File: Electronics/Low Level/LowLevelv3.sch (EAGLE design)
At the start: 66 parts, among them IC1_2515 MCP2515, IC2_2551 MCP2551DIL08, IC3_4802 MCP4802, Q1 16MHz, T1 2N3904, T2 2N3904, X1 284512-4, X3 Motor, X4 CLICK

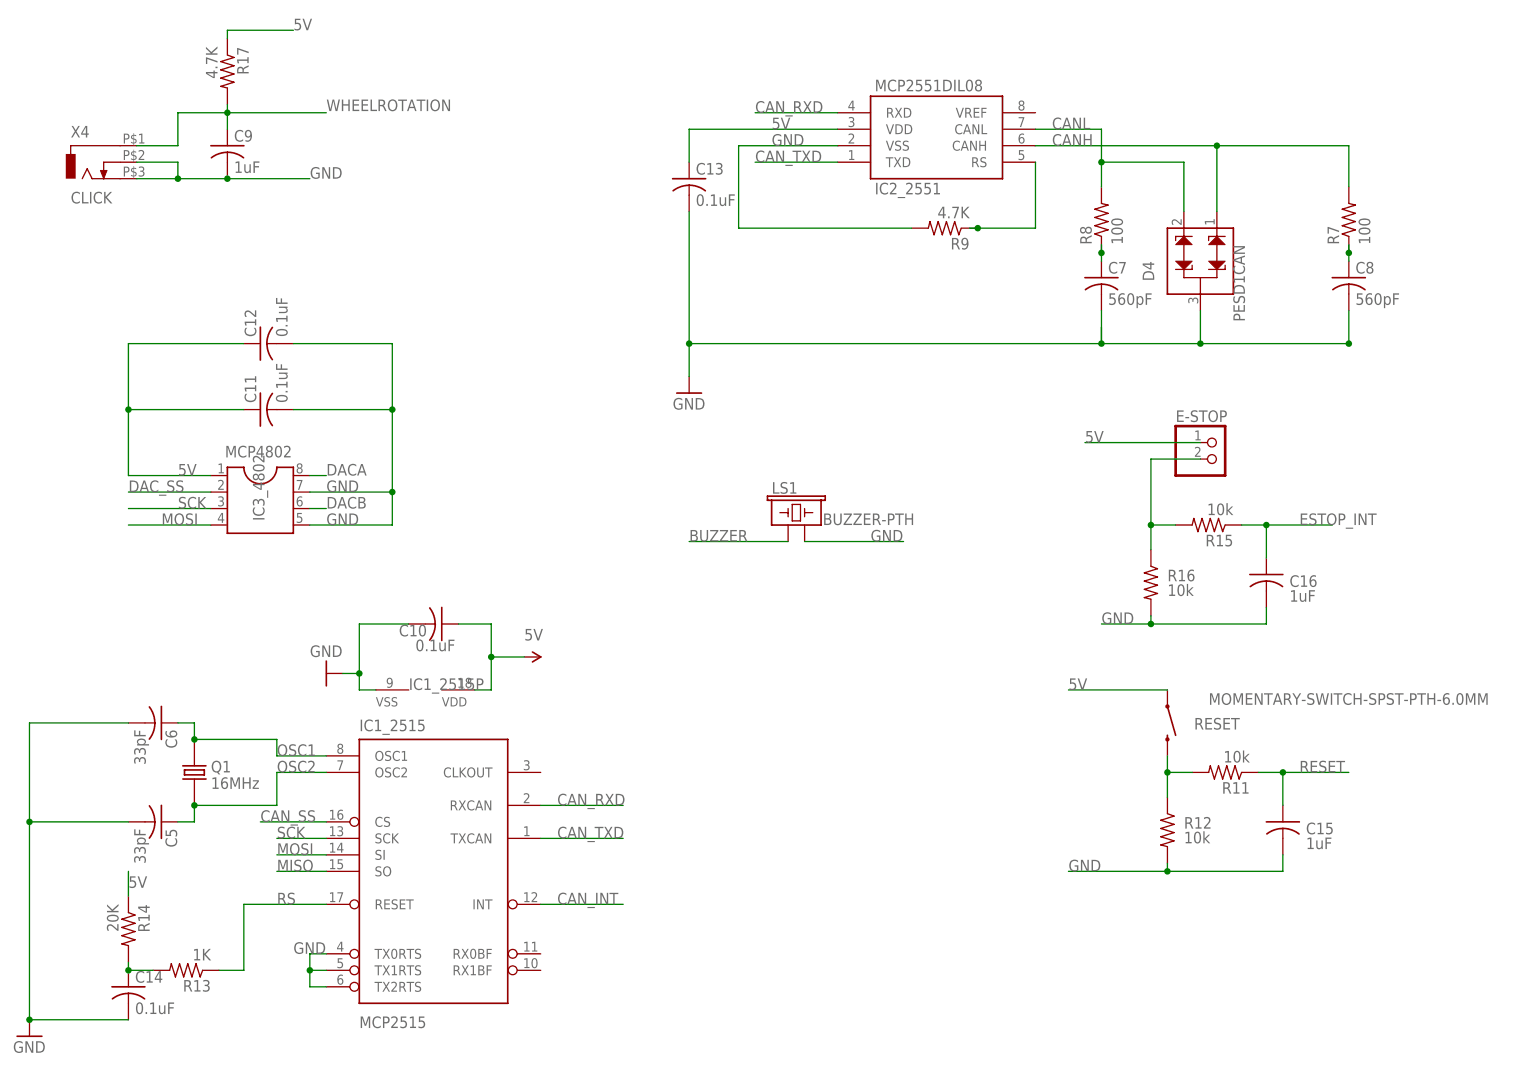
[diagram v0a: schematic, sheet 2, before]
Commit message: LLBv3 corrections
Fixed silk-via overlapping regions.
Fixed reset button schematic/wiring, now connects reset to ground.
Swapped CAN differential pair pinout by fixing the part in the library and re-routing the board.
Moved some surface mount parts to better propagate the ground plane.

Added on-silkscreen documentation for CAN and relay pinouts.
Added power-OK led and its resistor.
Changed board outline, reduced area and added two corner cuts.
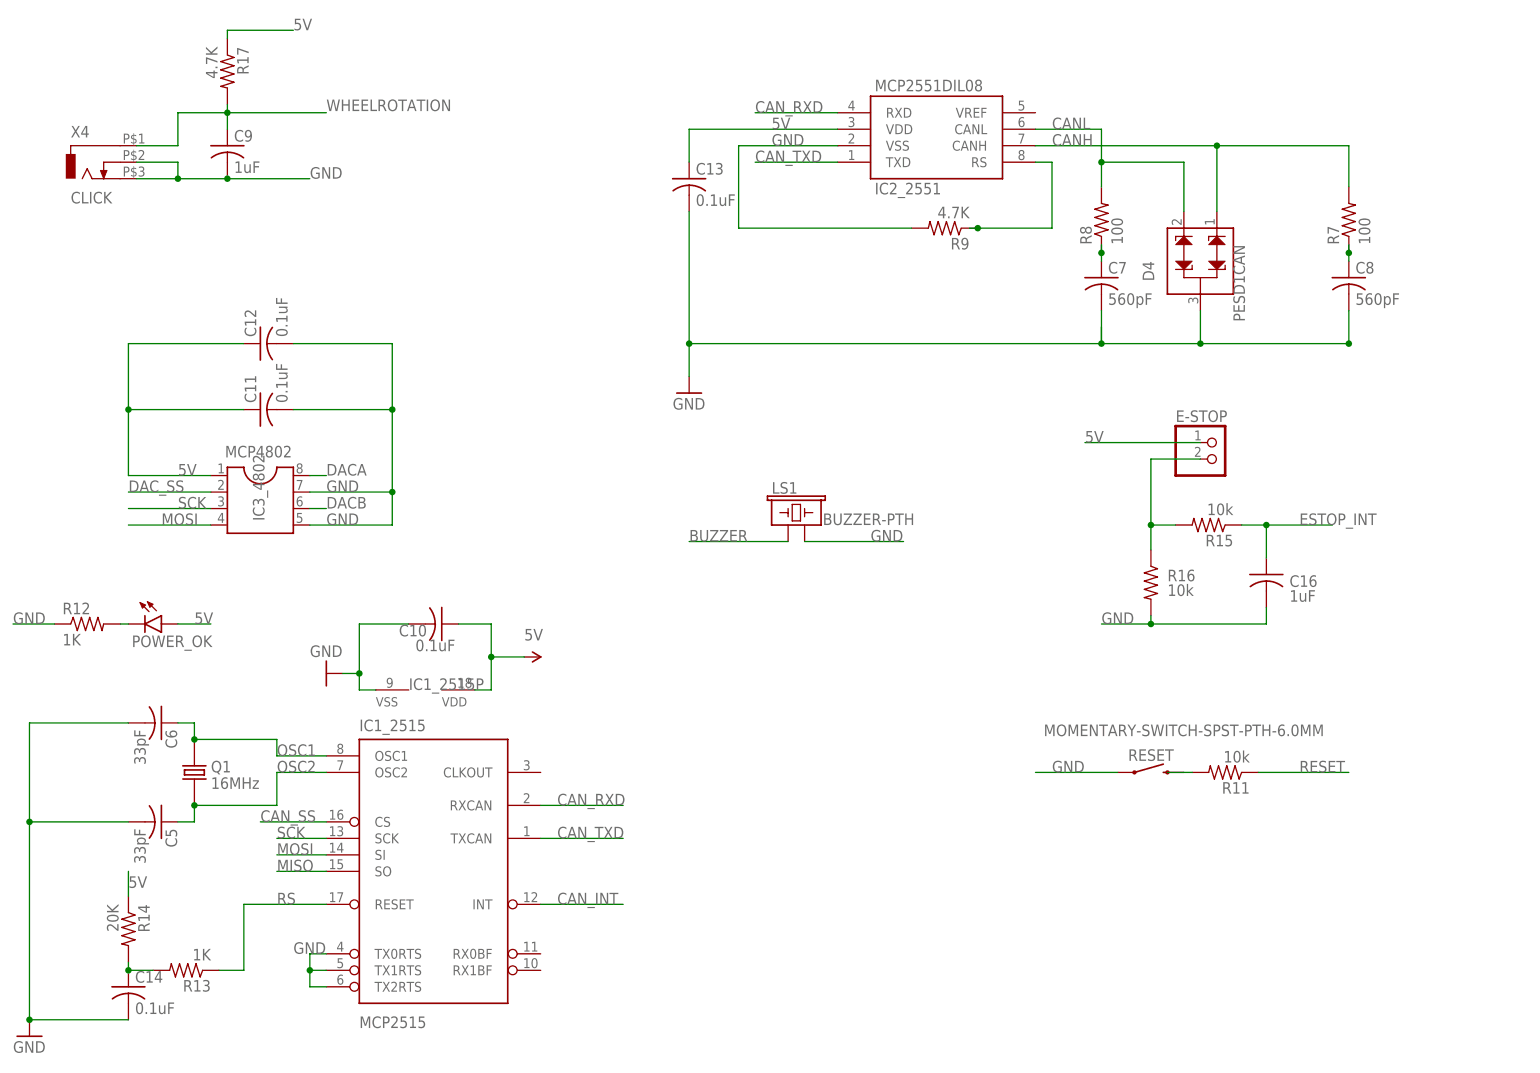
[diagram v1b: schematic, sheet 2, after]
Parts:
- removed C15: 1uF, resistor:C-USC1206
- added POWER_OK: (no value), led:LED3MM
- ICSP: value ICSP -> 2x3
- R12: value 10k -> 1K
- renumbered CANBUS to CAN/UART
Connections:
- new net N$11: POWER_OK.C, R12.2
- net 12V: now also X1.4; no longer X1.1
- net 24V: now also X1.3; no longer X1.2
- net 5V: now also POWER_OK.A; no longer RESET.1
- net GND: now also R12.1, RESET.1; no longer C15.2, R12.2
- net N$1: no longer R12.1
- net RESET: no longer C15.1
- net SOLENOID_COMMON: now also X1.1; no longer X1.4
- net SOLENOID_OUT: now also X1.2; no longer X1.3
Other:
- moved on the sheet: D1, R12, RESET, X1

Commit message: LLBv3.1 changes
Rerouted high-current relay circuit to handle swapped NC/NO pins.
Replaced 10-pin connector with 8-pin RJ45 modular jack. Expensive mistake.
Added debug LED on pin D13.
Added test points for steering header.
Silkscreen and routing corrections.
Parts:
- removed C2, C4: 1uF, resistor:C-USC1206
- removed R4: 4.7K, resistor:R-US_R1206
- removed STEERING_IO: 5-104069-4, elcanoParts:5-104069-4
- added DEBUG: (no value), led:LED3MM
- added STEERING: RJ45-8L-B, elcanoParts:RJ45-8L-B
- added TP1, TP2, TP3, TP4, TP5: PTR1PAD1-17, testpad:PTR1PAD1-17
- R2: value 4.7K -> 1K
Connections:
- removed net L_RET: R2.2, STEERING_IO.1
- removed net L_RTN_GND: ADCL.2, C2.1, R2.1
- removed net R_RET: R4.2, STEERING_IO.7
- removed net R_RTN_GND: ADCL.1, C4.1, R4.1
- new net DEBUG_LED: DEBUG.A, DIGITAL_8-13.6
- new net N$5: DEBUG.C, R2.2
- net 12V: now also PB2_12/24.NO, X1.3; no longer PB2_12/24.NC, X1.4
- net 24V: now also PB2_12/24.NC, X1.4; no longer PB2_12/24.NO, X1.3
- net 5V: now also STEERING.7, STEERING.8, TP5.TP; no longer STEERING_IO.10, STEERING_IO.4
- net GND: now also R2.1, STEERING.1, STEERING.3, STEERING.5, TP4.TP; no longer C2.2, C4.2, STEERING_IO.3, STEERING_IO.6, STEERING_IO.9
- net L_SENSE: now also TP1.TP
- net L_STR: now also STEERING.2; no longer STEERING_IO.2
- net R_SENSE: now also TP2.TP
- net R_STR: now also STEERING.4; no longer STEERING_IO.8
- net SOLENOID_COMMON: now also PB1_BRAKE_ON.NO; no longer PB1_BRAKE_ON.NC
- net SOLENOID_POWER: now also PB1_BRAKE_ON.NC; no longer PB1_BRAKE_ON.NO
- net STEER_SERVO_PWM: now also STEERING.6, TP3.TP; no longer STEERING_IO.5
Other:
- note added: "Please note that the symbol used here has inverted NC/NO pins. Pin 5 should be NC, and pin 4 is NO."
- note added: "~Latch"
- moved on the sheet: C1, C3, R1, R3
